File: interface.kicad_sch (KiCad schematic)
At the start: 8 parts, among them J6 DA15_CONN

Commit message: date update
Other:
- title: M17 Remote Radio Unit - RF board -> Remote Radio Unit - RF board
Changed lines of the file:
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@@
   (paper "A3")
   (title_block
-    (title "M17 Remote Radio Unit - RF board")
-    (date "28-10-2023")
+    (title "Remote Radio Unit - RF board")
+    (date "30-10-2023")
     (rev "A")
     (company "M17 Project")

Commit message: MPN/PN update
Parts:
- C12: MPN (none) -> C0603C104M5RAC7411
- C14: MPN (none) -> C0603C102J5GAC7411
- C9: MPN (none) -> CL10B105KB8NQNC
- FB2: MPN (none) -> BLM18KG601SH1D
- J6: MPN (none) -> TSM-108-01-L-DV-P-TR
- R2: MPN (none) -> RT0603FRE0710KL; PN (none) -> RT0603FRE0710KL
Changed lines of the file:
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@@
       (effects (font (size 1.27 1.27)) hide)
     )
-    (property "PN" "" (at 124.46 111.76 0)
+    (property "PN" "RT0603FRE0710KL" (at 124.46 111.76 0)
+      (effects (font (size 1.27 1.27)) hide)
+    )
+    (property "MPN" "RT0603FRE0710KL" (at 124.46 111.76 0)
       (effects (font (size 1.27 1.27)) hide)
     )
@@
     )
     (property "PN" "TSM-108-01-L-DV-P-TR" (at 109.22 140.97 0)
+      (effects (font (size 1.27 1.27)) hide)
+    )
+    (property "MPN" "TSM-108-01-L-DV-P-TR" (at 109.22 140.97 0)
       (effects (font (size 1.27 1.27)) hide)
     )
@@
       (effects (font (size 1.27 1.27)) hide)
     )
-    (property "PN" "" (at 139.7 111.76 0)
+    (property "PN" "RT0603FRE0710KL" (at 139.7 111.76 0)
+      (effects (font (size 1.27 1.27)) hide)
+    )
+    (property "MPN" "RT0603FRE0710KL" (at 139.7 111.76 0)
       (effects (font (size 1.27 1.27)) hide)
     )
@@
       (effects (font (size 1.27 1.27)) hide)
     )
-    (property "PN" "" (at 132.08 111.76 0)
+    (property "PN" "RT0603FRE0710KL" (at 132.08 111.76 0)
+      (effects (font (size 1.27 1.27)) hide)
+    )
+    (property "MPN" "RT0603FRE0710KL" (at 132.08 111.76 0)
       (effects (font (size 1.27 1.27)) hide)
     )
@@
       (effects (font (size 1.27 1.27)) hide)
     )
+    (property "MPN" "C0603C102J5GAC7411" (at 292.1 134.62 0)
+      (effects (font (size 1.27 1.27)) hide)
+    )
     (pin "1")
     (pin "2")
@@
       (effects (font (size 1.27 1.27)) hide)
     )
+    (property "MPN" "CL10B105KB8NQNC" (at 271.78 134.62 0)
+      (effects (font (size 1.27 1.27)) hide)
+    )
     (pin "1")
     (pin "2")
@@
       (effects (font (size 1.27 1.27)) hide)
     )
+    (property "MPN" "BLM18KG601SH1D" (at 278.13 128.27 0)
+      (effects (font (size 1.27 1.27)) hide)
+    )
     (pin "1")
     (pin "2")
@@
       (effects (font (size 1.27 1.27)) hide)
     )
+    (property "MPN" "C0603C104M5RAC7411" (at 283.21 134.62 0)
+      (effects (font (size 1.27 1.27)) hide)
+    )

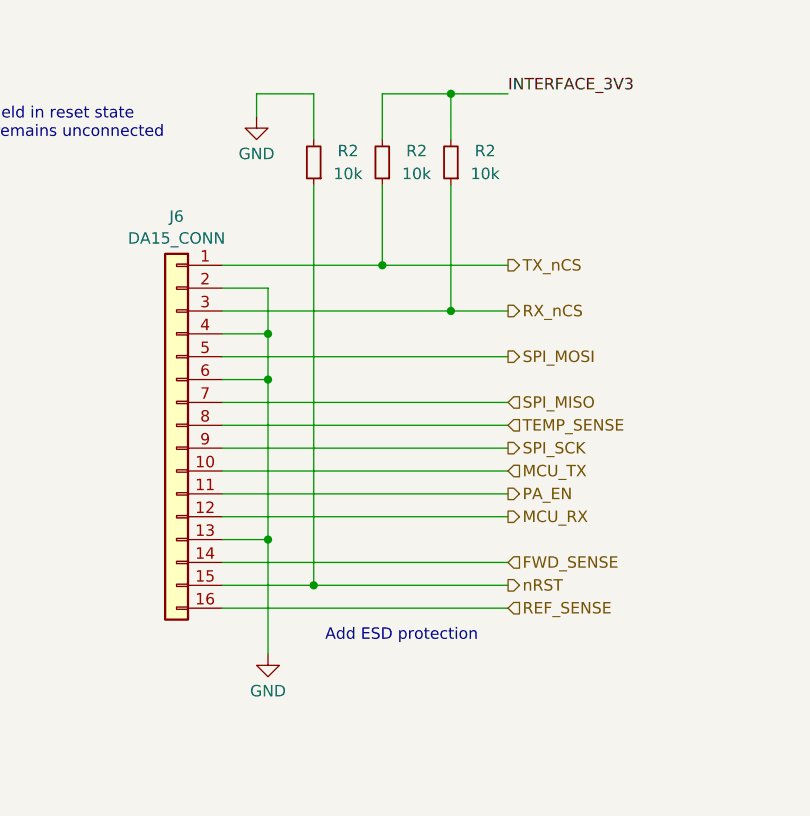
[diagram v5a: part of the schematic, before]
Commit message: WIP rev B
- replaced R44-R46 with 22k
- exposed BOOT0 at the DA15 connector
- added a testpoint at DAC OUT2
- added a buffer to the 40MHz reference oscillator
- removed C2
- bypassed R5 with a 100nF capacitor
- changed D5's voltage to 5.1V
- routed TX_SAMP_CLK
- changed temperature sensor's supply voltage to 5V
- added a series of 100p, 1n and 10n capacitors at PA_VGG
- reduced N-connector cutouts to 2.5mm
- improved RF output track a little
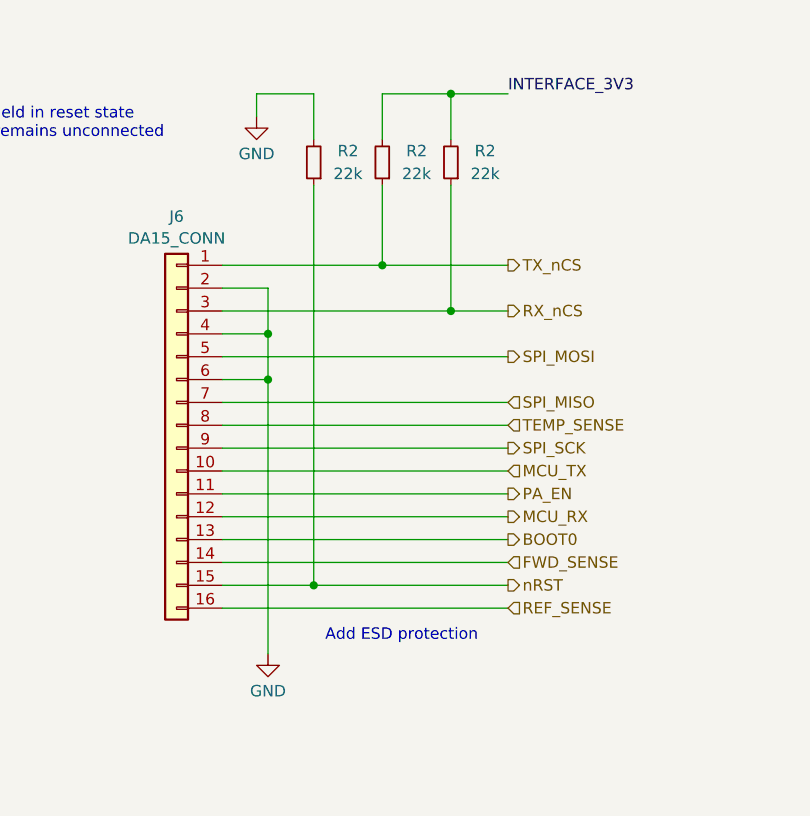
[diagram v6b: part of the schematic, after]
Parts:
- removed R2 (x3): 10k, Resistor_SMD:R_0603_1608Metric, symbol Device:R_Small
- added R2 (x3): 22k, Resistor_SMD:R_0603_1608Metric, symbol Device:R_Small
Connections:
- net GND: now also R2.2; no longer J6.13 (Pin_13)
- net INTERFACE_3V3: now also R2.2, R2.2
- net RX_nCS: now also R2.1
- net TX_nCS: now also R2.1
- net nRST: now also R2.1
- new net BOOT0: J6.13 (Pin_13)
